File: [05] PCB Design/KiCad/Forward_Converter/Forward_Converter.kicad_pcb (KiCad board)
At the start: 2 copper layers, 18 parts, among them Q1 CSD19534Q5A, Q2 CSD19534Q5A, Q3 BSC320N20NS3G, Q4 BCX56, Q5 BC857, T1 P0926NL, T2 EE30157-Custom, U1 LT1952EGN-1-PBF, U2 LTC3900ES8-PBF, U3 MC7812CDTRKG, U5 TCMT1106

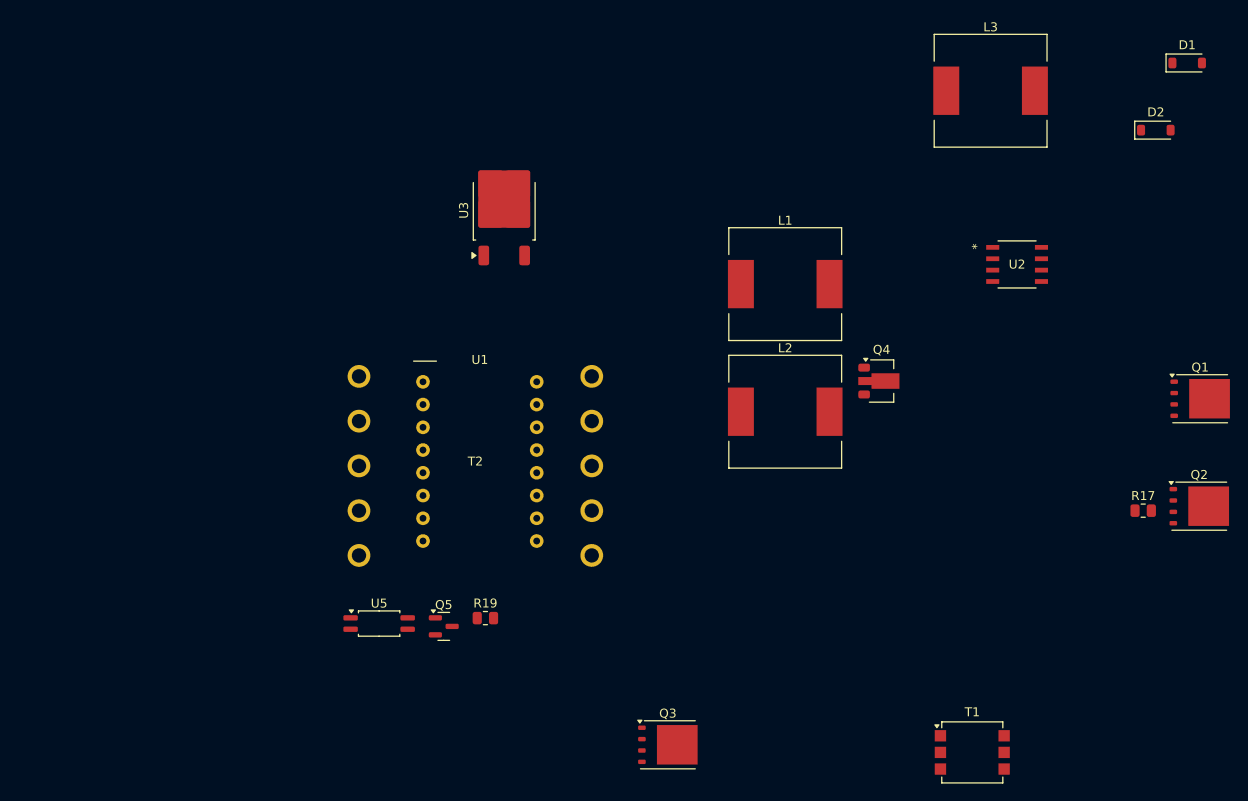
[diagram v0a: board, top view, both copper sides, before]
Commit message: Schematic Update
Almost Complete
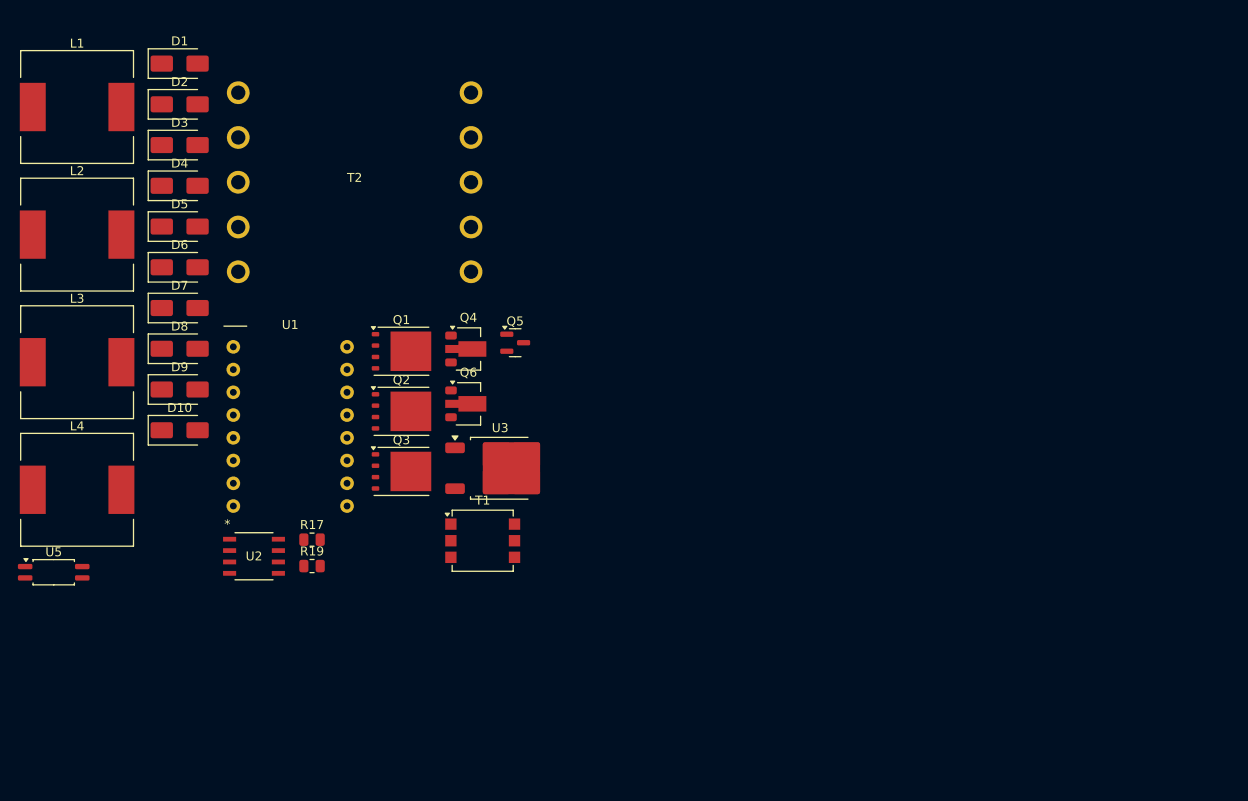
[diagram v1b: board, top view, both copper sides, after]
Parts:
- added D10: 1SMA5931, Diode_SMD:D_SMA, F.Cu at (58.5, 75.5)
- added D3: MS110, Diode_SMD:D_SMA, F.Cu at (58.5, 43.7)
- added D4: MS110, Diode_SMD:D_SMA, F.Cu at (58.5, 48.2)
- added D5: SMAJ7.5A, Diode_SMD:D_SMA, F.Cu at (58.5, 52.8)
- added D6: D_Schottky, Diode_SMD:D_SMA, F.Cu at (58.5, 57.3)
- added D7: D_Schottky, Diode_SMD:D_SMA, F.Cu at (58.5, 61.9)
- added D8: BR320, Diode_SMD:D_SMA, F.Cu at (58.5, 66.4)
- added D9: SMAJ7.5A, Diode_SMD:D_SMA, F.Cu at (58.5, 71.0)
- added L4: 22uH, Inductor_SMD:L_12x12mm_H6mm, F.Cu at (47.0, 82.2)
- added Q6: BCX56, Package_TO_SOT_SMD:SOT-89-3, F.Cu at (90.7, 72.6)
- D1, D2: value MBR0540 -> MS110; footprint Diode_SMD:D_SOD-123 -> Diode_SMD:D_SMA
- L3: value 10uH -> 22uH
- moved D1 112.5 mm to (58.5, 34.6)
- moved D2 109.1 mm to (58.5, 39.1)
- moved L3 106.4 mm to (47.0, 67.9)
- moved R17 92.9 mm to (73.3, 87.7)
- moved U2 91.2 mm to (66.8, 89.6)
- moved Q2 89.7 mm to (83.2, 73.4)
- moved Q1 89.4 mm to (83.2, 66.7)
- moved L1 81.5 mm to (47.0, 39.4)
- moved L2 81.5 mm to (47.0, 53.7)
- moved T1 59.6 mm to (92.3, 87.9)
- moved Q4 46.3 mm to (90.7, 66.4)
- moved Q3 42.6 mm to (83.2, 80.1)
- moved U5 36.8 mm to (44.4, 91.4)
- moved T2 34.4 mm to (78.0, 47.8)
- moved Q5 32.7 mm to (95.9, 65.7)
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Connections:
- net Net-(Q1-D) renamed /VSEC_GND
- net Net-(U3-VO) renamed /Vaux
- D1 pad 2: unconnected-(D1-A-Pad2) -> Net-(D1-A)
- D2 pad 1: Net-(D1-K) -> Net-(D2-K)
- D2 pad 2: GND -> GNDSEC
- L3 pad 1: Net-(U3-VI) -> /Vcont
- Q3 pad 5: Net-(Q3-D) -> /Vsw
- Q4 pad 1: unconnected-(Q4-B-Pad1) -> Net-(D5-A1)
- Q4 pad 2: unconnected-(Q4-C-Pad2) -> Net-(Q4-C)
- Q4 pad 3: unconnected-(Q4-E-Pad3) -> /Vbias
- T2 pad 1: unconnected-(T2-Pad1) -> Vin
- T2 pad 10: (no net) -> GNDSEC
- T2 pad 2: unconnected-(T2-Pad2) -> /Vsw
- T2 pad 3: Vin -> /RST
- T2 pad 4: Net-(Q3-D) -> /AUX
- T2 pad 5: Vin -> Net-(D1-A)
- T2 pad 6: unconnected-(T2-Pad6) -> (no net)
- T2 pad 9: (no net) -> unconnected-(T2-Pad9)
- U5 pad 2: Net-(Q5-E) -> GNDSEC
- U5 pad 3: GNDSEC -> Net-(Q5-E)

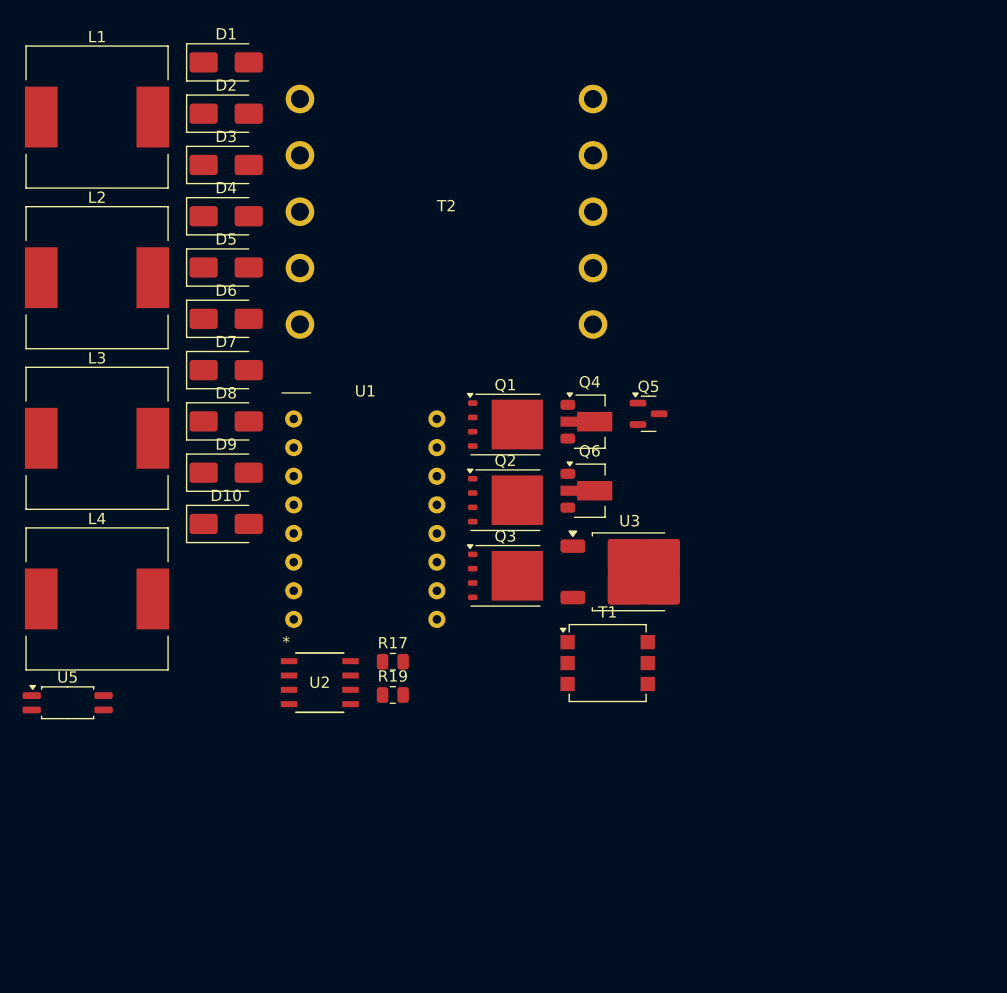
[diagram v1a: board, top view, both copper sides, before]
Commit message: Schematic Final with footprints
Layout to be done
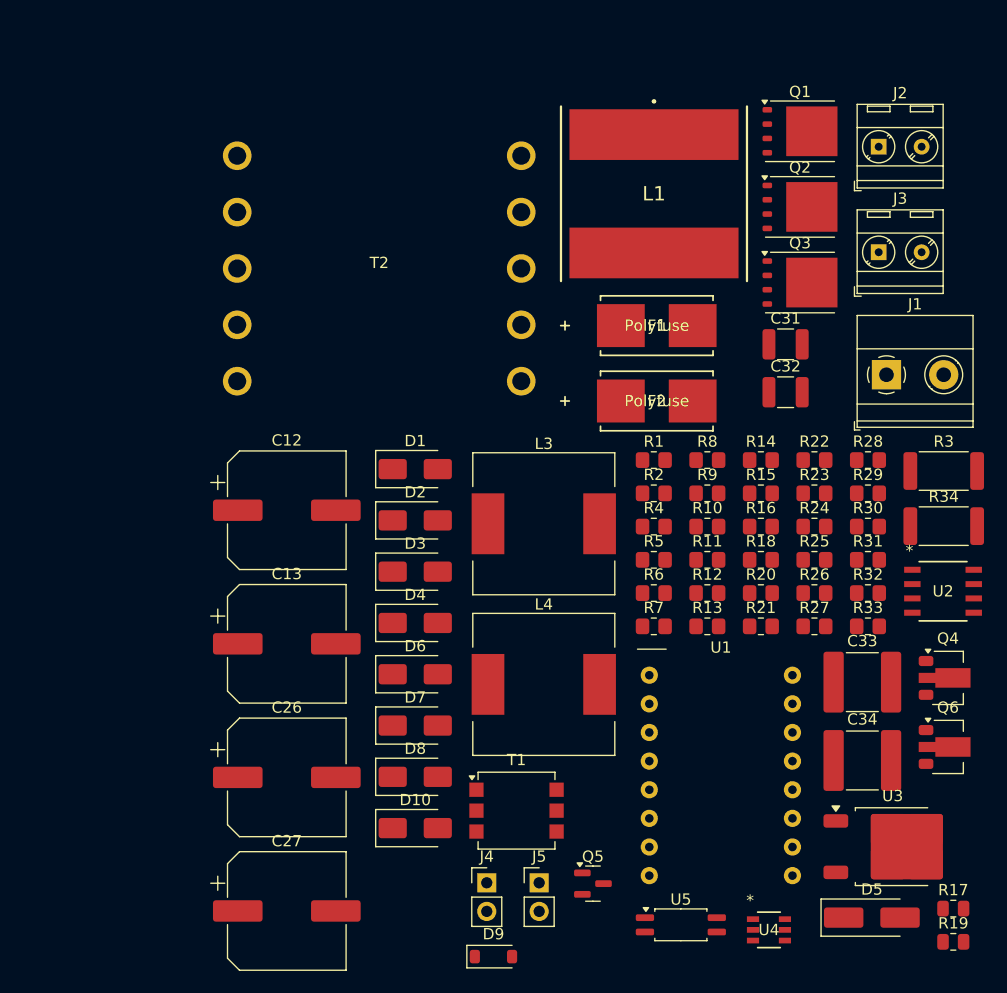
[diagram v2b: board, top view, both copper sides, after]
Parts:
- removed L2: 10uH, Inductor_SMD:L_12x12mm_H6mm
- added C12: 180u, Capacitor_SMD:CP_Elec_10x12.6, F.Cu at (63.9, 74.3)
- added C13: 180u, Capacitor_SMD:CP_Elec_10x12.6, F.Cu at (63.9, 86.2)
- added C26: 47u, Capacitor_SMD:CP_Elec_10x12.6, F.Cu at (63.9, 98.0)
- added C27: 47u, Capacitor_SMD:CP_Elec_10x12.6, F.Cu at (63.9, 109.8)
- added C31: 1uF, Capacitor_SMD:C_1210_3225Metric, F.Cu at (108.1, 59.6)
- added C32: 1uF, Capacitor_SMD:C_1210_3225Metric, F.Cu at (108.1, 63.8)
- added C33: 2.2u, Capacitor_SMD:C_2220_5750Metric, F.Cu at (114.9, 89.5)
- added C34: 2.2u, Capacitor_SMD:C_2220_5750Metric, F.Cu at (114.9, 96.5)
- added F1: Polyfuse, Forward_Footprint:0154010.DR, F.Cu at (96.7, 57.9)
- added F2: Polyfuse, Forward_Footprint:0154010.DR, F.Cu at (96.7, 64.6)
- added J1: Conn_01x02_Pin, TerminalBlock_Phoenix:TerminalBlock_Phoenix_MKDS-1,5-2-5.08_1x02_P5.08mm_Horizontal, F.Cu at (117.0, 62.3)
- added J2: Conn_01x02_Pin, TerminalBlock_MetzConnect:TerminalBlock_MetzConnect_Type086_RT03402HBLC_1x02_P3.81mm_Horizontal, F.Cu at (116.4, 42.0)
- added J3: Conn_01x02_Pin, TerminalBlock_MetzConnect:TerminalBlock_MetzConnect_Type086_RT03402HBLC_1x02_P3.81mm_Horizontal, F.Cu at (116.4, 51.4)
- added J4: Conn_01x02_Pin, Connector_PinHeader_2.54mm:PinHeader_1x02_P2.54mm_Vertical, F.Cu at (81.6, 107.3)
- added J5: Conn_01x02_Pin, Connector_PinHeader_2.54mm:PinHeader_1x02_P2.54mm_Vertical, F.Cu at (86.2, 107.3)
- added R1: 12R, Resistor_SMD:R_0805_2012Metric_Pad1.20x1.40mm_HandSolder, F.Cu at (96.4, 69.8)
- added R10: 180k, Resistor_SMD:R_0805_2012Metric_Pad1.20x1.40mm_HandSolder, F.Cu at (101.2, 75.8)
- added R11: 100k, Resistor_SMD:R_0805_2012Metric_Pad1.20x1.40mm_HandSolder, F.Cu at (101.2, 78.7)
- added R12: 160k, Resistor_SMD:R_0805_2012Metric_Pad1.20x1.40mm_HandSolder, F.Cu at (101.2, 81.7)
- added R13: 10k, Resistor_SMD:R_0805_2012Metric_Pad1.20x1.40mm_HandSolder, F.Cu at (101.2, 84.6)
- added R14: 10k, Resistor_SMD:R_0805_2012Metric_Pad1.20x1.40mm_HandSolder, F.Cu at (105.9, 69.8)
- added R15: 10k, Resistor_SMD:R_0805_2012Metric_Pad1.20x1.40mm_HandSolder, F.Cu at (105.9, 72.8)
- added R16: 25, Resistor_SMD:R_0805_2012Metric_Pad1.20x1.40mm_HandSolder, F.Cu at (105.9, 75.8)
- added R18: 25, Resistor_SMD:R_0805_2012Metric_Pad1.20x1.40mm_HandSolder, F.Cu at (105.9, 78.7)
- added R2: 10k, Resistor_SMD:R_0805_2012Metric_Pad1.20x1.40mm_HandSolder, F.Cu at (96.4, 72.8)
- added R20: 47R, Resistor_SMD:R_0805_2012Metric_Pad1.20x1.40mm_HandSolder, F.Cu at (105.9, 81.7)
- added R21: 200k, Resistor_SMD:R_0805_2012Metric_Pad1.20x1.40mm_HandSolder, F.Cu at (105.9, 84.6)
- added R22: 27k, Resistor_SMD:R_0805_2012Metric_Pad1.20x1.40mm_HandSolder, F.Cu at (110.7, 69.8)
- added R23: 8.2k, Resistor_SMD:R_0805_2012Metric_Pad1.20x1.40mm_HandSolder, F.Cu at (110.7, 72.8)
- added R24: 4.7k, Resistor_SMD:R_0805_2012Metric_Pad1.20x1.40mm_HandSolder, F.Cu at (110.7, 75.8)
- added R25: 1.2k, Resistor_SMD:R_0805_2012Metric_Pad1.20x1.40mm_HandSolder, F.Cu at (110.7, 78.7)
- added R26: 220R, Resistor_SMD:R_0805_2012Metric_Pad1.20x1.40mm_HandSolder, F.Cu at (110.7, 81.7)
- added R27: 10k, Resistor_SMD:R_0805_2012Metric_Pad1.20x1.40mm_HandSolder, F.Cu at (110.7, 84.6)
- added R28: 1k, Resistor_SMD:R_0805_2012Metric_Pad1.20x1.40mm_HandSolder, F.Cu at (115.4, 69.8)
- added R29: 4.7k, Resistor_SMD:R_0805_2012Metric_Pad1.20x1.40mm_HandSolder, F.Cu at (115.4, 72.8)
- added R3: 15m, Resistor_SMD:R_2512_6332Metric, F.Cu at (122.1, 70.8)
- added R30: 4.7k, Resistor_SMD:R_0805_2012Metric_Pad1.20x1.40mm_HandSolder, F.Cu at (115.4, 75.8)
- added R31: 0R, Resistor_SMD:R_0805_2012Metric_Pad1.20x1.40mm_HandSolder, F.Cu at (115.4, 78.7)
- added R32: 0, Resistor_SMD:R_0805_2012Metric_Pad1.20x1.40mm_HandSolder, F.Cu at (115.4, 81.7)
- added R33: 0, Resistor_SMD:R_0805_2012Metric_Pad1.20x1.40mm_HandSolder, F.Cu at (115.4, 84.6)
- added R34: 15m, Resistor_SMD:R_2512_6332Metric, F.Cu at (122.1, 75.7)
- added R4: 12k, Resistor_SMD:R_0805_2012Metric_Pad1.20x1.40mm_HandSolder, F.Cu at (96.4, 75.8)
- added R5: 10k, Resistor_SMD:R_0805_2012Metric_Pad1.20x1.40mm_HandSolder, F.Cu at (96.4, 78.7)
- added R6: 240k, Resistor_SMD:R_0805_2012Metric_Pad1.20x1.40mm_HandSolder, F.Cu at (96.4, 81.7)
- added R7: 18k, Resistor_SMD:R_0805_2012Metric_Pad1.20x1.40mm_HandSolder, F.Cu at (96.4, 84.6)
- added R8: 47R, Resistor_SMD:R_0805_2012Metric_Pad1.20x1.40mm_HandSolder, F.Cu at (101.2, 69.8)
- added R9: 10k, Resistor_SMD:R_0805_2012Metric_Pad1.20x1.40mm_HandSolder, F.Cu at (101.2, 72.8)
- added U4: LT4430ES6-TRPBF, Forward_Footprint:TSOT-23_S6_LIT-M, F.Cu at (106.6, 111.5)
- D5: value SMAJ7.5A -> SMAJ4737A; footprint Diode_SMD:D_SMA -> Diode_SMD:D_SMA_Handsoldering
- D9: value SMAJ7.5A -> BZT52C12-TP; footprint Diode_SMD:D_SMA -> Diode_SMD:D_SOD-123
- L1: value 10uH -> 22uH; footprint Inductor_SMD:L_12x12mm_H6mm -> Forward_Footprint:SRP1513CA8R2M_V2
- R17, R19: value 10k -> 22k
- moved D5 81.3 mm to (115.8, 110.4)
- moved U5 57.9 mm to (98.8, 111.1)
- moved U2 55.9 mm to (122.1, 81.5)
- moved R17 54.3 mm to (123.0, 109.6)
- moved R19 54.3 mm to (123.0, 112.6)
- moved L1 49.9 mm to (96.4, 46.2)
- moved D9 49.0 mm to (82.2, 113.9)
- moved Q5 42.0 mm to (91.0, 107.4)
- moved L3 40.4 mm to (86.7, 75.5)
- moved L4 40.4 mm to (86.7, 89.8)
- moved D1 39.8 mm to (75.2, 70.7)
- moved D2 39.8 mm to (75.2, 75.2)
- moved D3 39.8 mm to (75.2, 79.8)
- moved D4 39.8 mm to (75.2, 84.3)
- moved Q4 39.1 mm to (122.5, 89.2)
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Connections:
- net /VSEC renamed /VSEC+
- net /VSEC_GND renamed /VSEC-
- D1 pad 2: Net-(D1-A) -> GND
- D10 pad 2: Net-(D1-A) -> GND
- D3 pad 2: unconnected-(D3-A-Pad2) -> /Vaux
- D8 pad 2: GND -> PGND
- D9 pad 2: Net-(D1-A) -> GND
- L1 pad 2: Net-(L1-Pad2) -> /5V
- L3 pad 1: /Vcont -> Net-(Q6-C)
- L4 pad 1: Net-(Q4-C) -> Net-(U3-VO)
- Q1 pad 1: GNDSEC -> GNDPWR
- Q1 pad 2: GNDSEC -> GNDPWR
- Q1 pad 3: GNDSEC -> GNDPWR
- Q2 pad 1: GNDSEC -> GNDPWR
- Q2 pad 2: GNDSEC -> GNDPWR
- Q2 pad 3: GNDSEC -> GNDPWR
- Q4 pad 2: Net-(Q4-C) -> /12V
- Q4 pad 3: /Vbias -> /8V
- Q6 pad 2: /Vcont -> Net-(Q6-C)
- R17 pad 2: GNDSEC -> GNDPWR
- R19 pad 2: GNDSEC -> GNDPWR
- T2 pad 5: Net-(D1-A) -> GND
- T2 pad 9: unconnected-(T2-Pad9) -> /Vaux
- U1 pad 11: Net-(U1-ISENSE) -> Net-(U1-OC)
- U1 pad 15: /Vcont -> /Vbias
- U2 pad 4: /Vbias -> /8V
- U3 pad 1: Net-(U3-VI) -> /12V
- U3 pad 2: GND -> GNDSEC
- U3 pad 3: /Vaux -> Net-(U3-VO)
